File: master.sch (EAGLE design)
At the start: 31 parts, among them IC1 ATMEGA328-P, U2 ENC28J60-SO, Y2 25MHz, Y3 16MHz

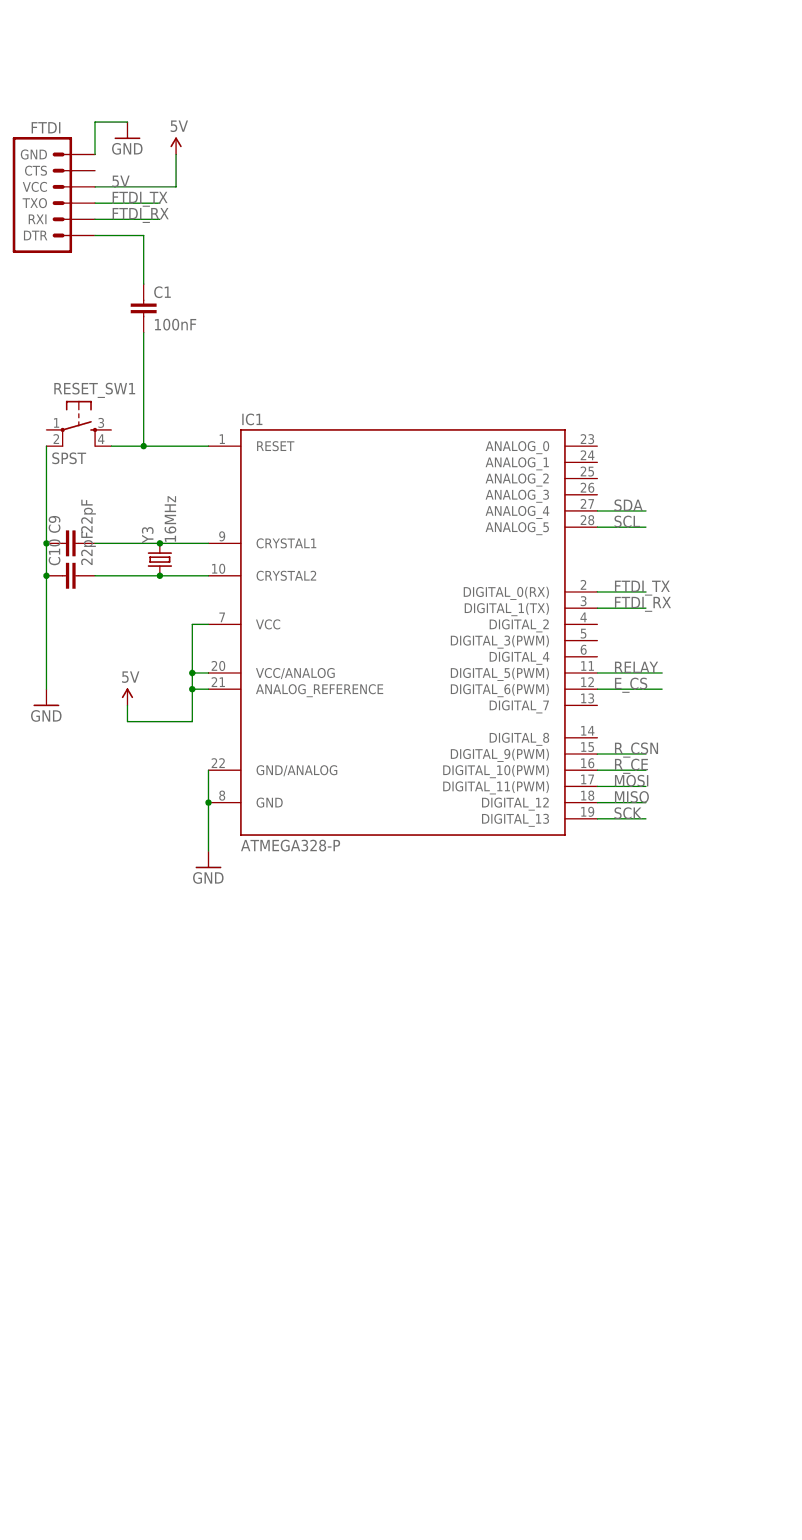
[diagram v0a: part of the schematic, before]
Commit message: Use SMD Atmega
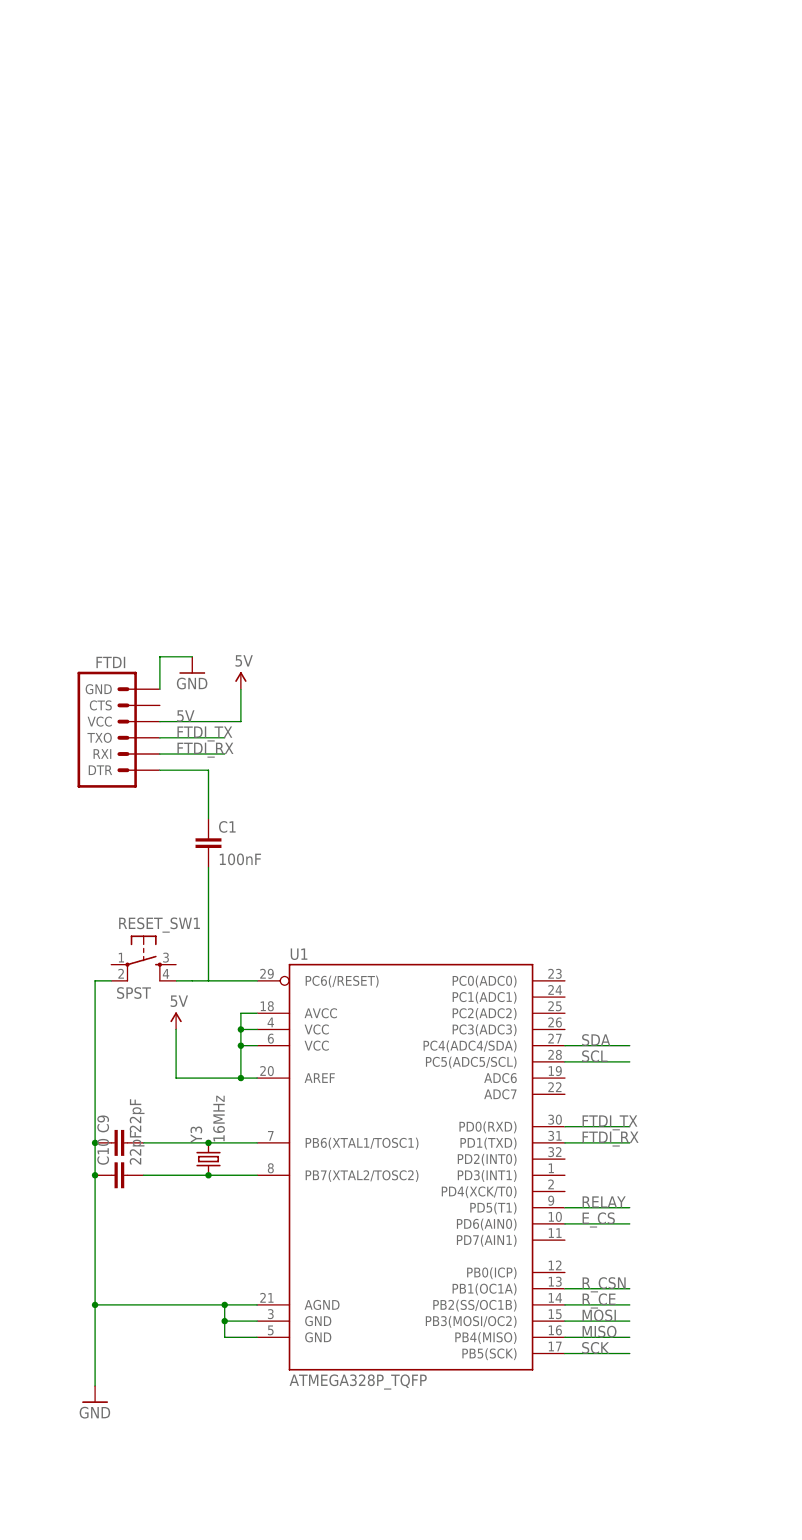
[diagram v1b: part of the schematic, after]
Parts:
- removed IC1: ATMEGA328-P, Arduino-AVR:ATMEGA168-PU
- added U1: ATMEGA328P_TQFP, SparkFun-DigitalIC:ATMEGA328P_TQFP
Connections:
- net 5V: now also U1.AREF, U1.AVCC, U1.VCC@4, U1.VCC@6; no longer IC1.ANALOG_REFERENCE, IC1.VCC, IC1.VCC/ANALOG
- net E_CS: now also U1.PD6(AIN0); no longer IC1.DIGITAL_6(PWM)
- net FTDI_RX: now also U1.PD1(TXD); no longer IC1.DIGITAL_1(TX)
- net FTDI_TX: now also U1.PD0(RXD); no longer IC1.DIGITAL_0(RX)
- net GND: now also U1.AGND, U1.GND@3, U1.GND@5; no longer IC1.GND, IC1.GND/ANALOG
- net MISO: now also U1.PB4(MISO); no longer IC1.DIGITAL_12
- net MOSI: now also U1.PB3(MOSI/OC2); no longer IC1.DIGITAL_11(PWM)
- net N$20: now also U1.PB6(XTAL1/TOSC1); no longer IC1.CRYSTAL1
- net N$21: now also U1.PB7(XTAL2/TOSC2); no longer IC1.CRYSTAL2
- net RELAY: now also U1.PD5(T1); no longer IC1.DIGITAL_5(PWM)
- net RESET: now also U1.PC6(/RESET); no longer IC1.RESET
- net R_CE: now also U1.PB2(SS/OC1B); no longer IC1.DIGITAL_10(PWM)
- net R_CSN: now also U1.PB1(OC1A); no longer IC1.DIGITAL_9(PWM)
- net SCK: now also U1.PB5(SCK); no longer IC1.DIGITAL_13
- net SCL: now also U1.PC5(ADC5/SCL); no longer IC1.ANALOG_5
- net SDA: now also U1.PC4(ADC4/SDA); no longer IC1.ANALOG_4
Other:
- moved on the sheet: C1, C10, C9, FTDI, RESET_SW1, Y3

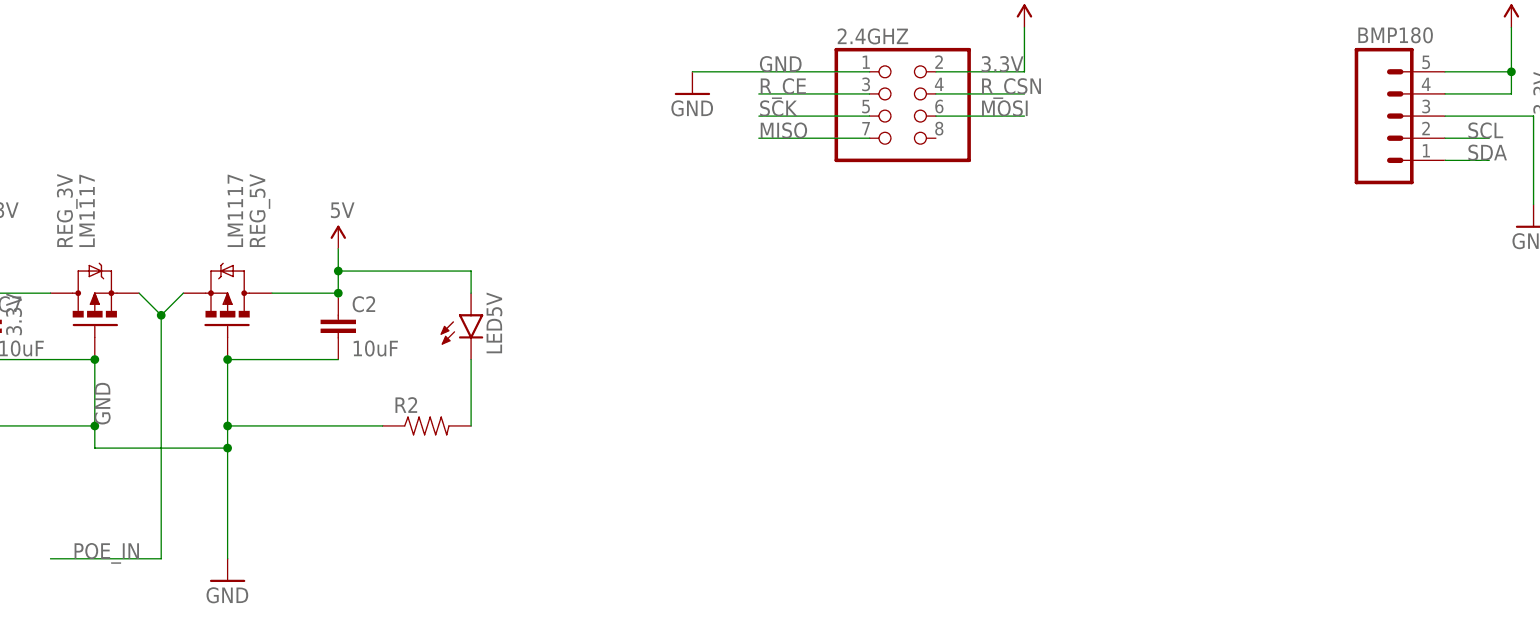
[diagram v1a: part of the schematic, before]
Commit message: Fix LM7805 pinout
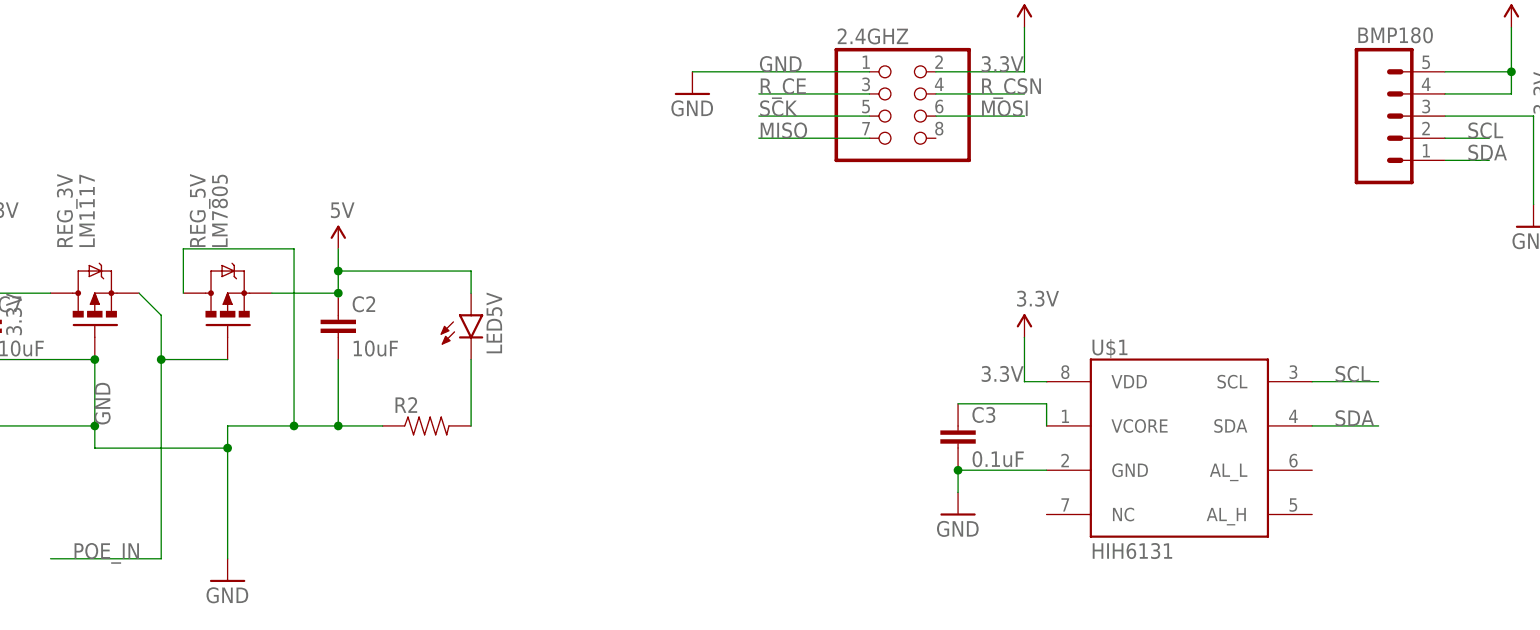
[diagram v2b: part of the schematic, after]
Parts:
- added C3: 0.1uF, SparkFun-Capacitors:CAPPTH
- added U$1: HIH6131, SparkFun-AnalogIC:HIH6131
- REG_5V: value LM1117 -> LM7805
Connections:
- new net N$17: C3.1, U$1.VCORE
- net 3.3V: now also U$1.VDD
- net 5V: now also REG_5V.S; no longer REG_5V.D
- net GND: now also C3.2, REG_5V.D, U$1.GND; no longer REG_5V.G
- net POE_IN: now also REG_5V.G; no longer REG_5V.S
- net SCL: now also U$1.SCL
- net SDA: now also U$1.SDA
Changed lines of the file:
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@@
 <part name="GND1" library="SparkFun-Aesthetics" deviceset="GND" device=""/>
 <part name="GND13" library="SparkFun-Aesthetics" deviceset="GND" device=""/>
-<part name="REG_5V" library="User-Submitted" deviceset="MOSFET-PCHANNEL" device="FQP27P06" value="LM1117"/>
 <part name="2.4GHZ" library="adafruit" deviceset="PINHD-2X4" device=""/>
 <part name="GND15" library="SparkFun-Aesthetics" deviceset="GND" device=""/>
@@
 <part name="U1" library="SparkFun-DigitalIC" deviceset="ATMEGA328P_TQFP" device="" value="ATMEGA328P_TQFP"/>
 <part name="SUPPLY9" library="SparkFun-Aesthetics" deviceset="5V" device=""/>
+<part name="U$1" library="SparkFun-AnalogIC" deviceset="HIH6131" device=""/>
+<part name="C3" library="SparkFun-Capacitors" deviceset="CAP" device="PTH" value="0.1uF"/>
+<part name="GND4" library="SparkFun-Aesthetics" deviceset="GND" device=""/>
+<part name="SUPPLY1" library="SparkFun-Aesthetics" deviceset="3.3V" device=""/>
+<part name="REG_5V" library="User-Submitted" deviceset="MOSFET-PCHANNEL" device="FQP27P06" value="LM7805"/>
 </parts>
 <sheets>
@@
 <instance part="GND1" gate="1" x="195.58" y="353.06"/>
 <instance part="GND13" gate="1" x="66.04" y="20.32"/>
-<instance part="REG_5V" gate="G$1" x="66.04" y="53.34" rot="MR90"/>
 <instance part="2.4GHZ" gate="A" x="142.24" y="73.66"/>
 <instance part="GND15" gate="1" x="119.38" y="76.2"/>
@@
 <instance part="U1" gate="U$1" x="48.26" y="147.32"/>
 <instance part="SUPPLY9" gate="G$1" x="10.16" y="170.18"/>
+<instance part="U$1" gate="G$1" x="175.26" y="35.56"/>
+<instance part="C3" gate="G$1" x="149.86" y="35.56"/>
+<instance part="GND4" gate="1" x="149.86" y="27.94"/>
+<instance part="SUPPLY1" gate="G$1" x="157.48" y="48.26"/>
+<instance part="REG_5V" gate="G$1" x="66.04" y="53.34" rot="R90"/>
 </instances>
 <busses>
@@
 <label x="50.8" y="43.18" size="1.778" layer="95" rot="R270"/>
 <wire x1="50.8" y1="38.1" x2="50.8" y2="45.72" width="0.1524" layer="91"/>
-<wire x1="66.04" y1="45.72" x2="78.74" y2="45.72" width="0.1524" layer="91"/>
-<pinref part="C2" gate="G$1" pin="2"/>
 <wire x1="66.04" y1="22.86" x2="66.04" y2="35.56" width="0.1524" layer="91"/>
-<wire x1="66.04" y1="45.72" x2="66.04" y2="38.1" width="0.1524" layer="91"/>
 <wire x1="66.04" y1="38.1" x2="66.04" y2="35.56" width="0.1524" layer="91"/>
 <wire x1="50.8" y1="35.56" x2="66.04" y2="35.56" width="0.1524" layer="91"/>
@@
 <junction x="50.8" y="38.1"/>
 <pinref part="R2" gate="G$1" pin="1"/>
-<wire x1="83.82" y1="38.1" x2="66.04" y2="38.1" width="0.1524" layer="91"/>
-<junction x="66.04" y="38.1"/>
+<wire x1="83.82" y1="38.1" x2="78.74" y2="38.1" width="0.1524" layer="91"/>
 <pinref part="GND13" gate="1" pin="GND"/>
-<pinref part="REG_5V" gate="G$1" pin="G"/>
-<junction x="66.04" y="45.72"/>
+<wire x1="78.74" y1="38.1" x2="73.66" y2="38.1" width="0.1524" layer="91"/>
+<wire x1="73.66" y1="38.1" x2="66.04" y2="38.1" width="0.1524" layer="91"/>
+<wire x1="60.96" y1="53.34" x2="60.96" y2="58.42" width="0.1524" layer="91"/>
+<wire x1="60.96" y1="58.42" x2="73.66" y2="58.42" width="0.1524" layer="91"/>
+<wire x1="73.66" y1="58.42" x2="73.66" y2="38.1" width="0.1524" layer="91"/>
+<junction x="73.66" y="38.1"/>
+<pinref part="C2" gate="G$1" pin="2"/>
+<wire x1="78.74" y1="45.72" x2="78.74" y2="38.1" width="0.1524" layer="91"/>
+<junction x="78.74" y="38.1"/>
+<pinref part="REG_5V" gate="G$1" pin="D"/>
 </segment>
 <segment>
@@
 <junction x="17.78" y="124.46"/>
 </segment>
+<segment>
+<pinref part="U$1" gate="G$1" pin="GND"/>
+<wire x1="160.02" y1="33.02" x2="149.86" y2="33.02" width="0.1524" layer="91"/>
+<pinref part="C3" gate="G$1" pin="2"/>
+<pinref part="GND4" gate="1" pin="GND"/>
+<wire x1="149.86" y1="33.02" x2="149.86" y2="30.48" width="0.1524" layer="91"/>
+<junction x="149.86" y="33.02"/>
+</segment>
 </net>
 <net name="E_CS" class="0">
@@
 <label x="73.66" y="165.1" size="1.778" layer="95"/>
 </segment>
+<segment>
+<pinref part="U$1" gate="G$1" pin="SCL"/>
+<wire x1="190.5" y1="43.18" x2="198.12" y2="43.18" width="0.1524" layer="91"/>
+<label x="193.04" y="43.18" size="1.778" layer="95"/>
+</segment>
 </net>
 <net name="SDA" class="0">
@@
 <wire x1="81.28" y1="167.64" x2="71.12" y2="167.64" width="0.1524" layer="91"/>
 <label x="73.66" y="167.64" size="1.778" layer="95"/>
+</segment>
+<segment>
+<pinref part="U$1" gate="G$1" pin="SDA"/>
+<wire x1="198.12" y1="38.1" x2="190.5" y2="38.1" width="0.1524" layer="91"/>
+<label x="193.04" y="38.1" size="1.778" layer="95"/>
 </segment>
 </net>
@@
 <wire x1="284.48" y1="299.72" x2="284.48" y2="304.8" width="0.1524" layer="91"/>
 </segment>
+<segment>
+<pinref part="U$1" gate="G$1" pin="VDD"/>
+<pinref part="SUPPLY1" gate="G$1" pin="3.3V"/>
+<wire x1="160.02" y1="43.18" x2="157.48" y2="43.18" width="0.1524" layer="91"/>
+<wire x1="157.48" y1="43.18" x2="157.48" y2="48.26" width="0.1524" layer="91"/>
+<label x="152.4" y="43.18" size="1.778" layer="95"/>
+</segment>
 </net>
 <net name="5V" class="0">
@@
 <pinref part="C2" gate="G$1" pin="1"/>
 <wire x1="78.74" y1="53.34" x2="78.74" y2="55.88" width="0.1524" layer="91"/>
-<pinref part="REG_5V" gate="G$1" pin="D"/>
 <wire x1="71.12" y1="53.34" x2="78.74" y2="53.34" width="0.1524" layer="91"/>
 <junction x="78.74" y="53.34"/>
+<pinref part="REG_5V" gate="G$1" pin="S"/>
 </segment>
 <segment>
@@
 <net name="POE_IN" class="0">
 <segment>
-<wire x1="60.96" y1="53.34" x2="58.42" y2="50.8" width="0.1524" layer="91"/>
-<wire x1="58.42" y1="50.8" x2="58.42" y2="22.86" width="0.1524" layer="91"/>
+<wire x1="58.42" y1="50.8" x2="58.42" y2="45.72" width="0.1524" layer="91"/>
 <pinref part="REG_3V" gate="G$1" pin="S"/>
+<wire x1="58.42" y1="45.72" x2="58.42" y2="22.86" width="0.1524" layer="91"/>
 <wire x1="58.42" y1="50.8" x2="55.88" y2="53.34" width="0.1524" layer="91"/>
-<junction x="58.42" y="50.8"/>
 <wire x1="45.72" y1="22.86" x2="58.42" y2="22.86" width="0.1524" layer="91"/>
 <label x="48.26" y="22.86" size="1.778" layer="95"/>
-<pinref part="REG_5V" gate="G$1" pin="S"/>
+<wire x1="66.04" y1="45.72" x2="58.42" y2="45.72" width="0.1524" layer="91"/>
+<junction x="58.42" y="45.72"/>
+<pinref part="REG_5V" gate="G$1" pin="G"/>
 </segment>
 <segment>
@@
 </segment>
 </net>
+<net name="N$17" class="0">
+<segment>
+<pinref part="C3" gate="G$1" pin="1"/>
+<pinref part="U$1" gate="G$1" pin="VCORE"/>
+<wire x1="149.86" y1="40.64" x2="160.02" y2="40.64" width="0.1524" layer="91"/>
+<wire x1="160.02" y1="40.64" x2="160.02" y2="38.1" width="0.1524" layer="91"/>
+</segment>
+</net>
